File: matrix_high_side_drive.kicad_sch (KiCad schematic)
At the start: 28 parts

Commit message: [#72133] Unify sheet size
Signed-off-by: Dawid Lentka <dlentka@antmicro.com>
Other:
- title: (none) -> LED Panel Board
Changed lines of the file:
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@@
 	(generator_version "8.0")
 	(paper "A4")
+	(title_block
+		(title "LED Panel Board")
+		(date "28.01.2025")
+		(rev "1.0.0")
+	)
 	(junction
 		(at 58.42 41.91)

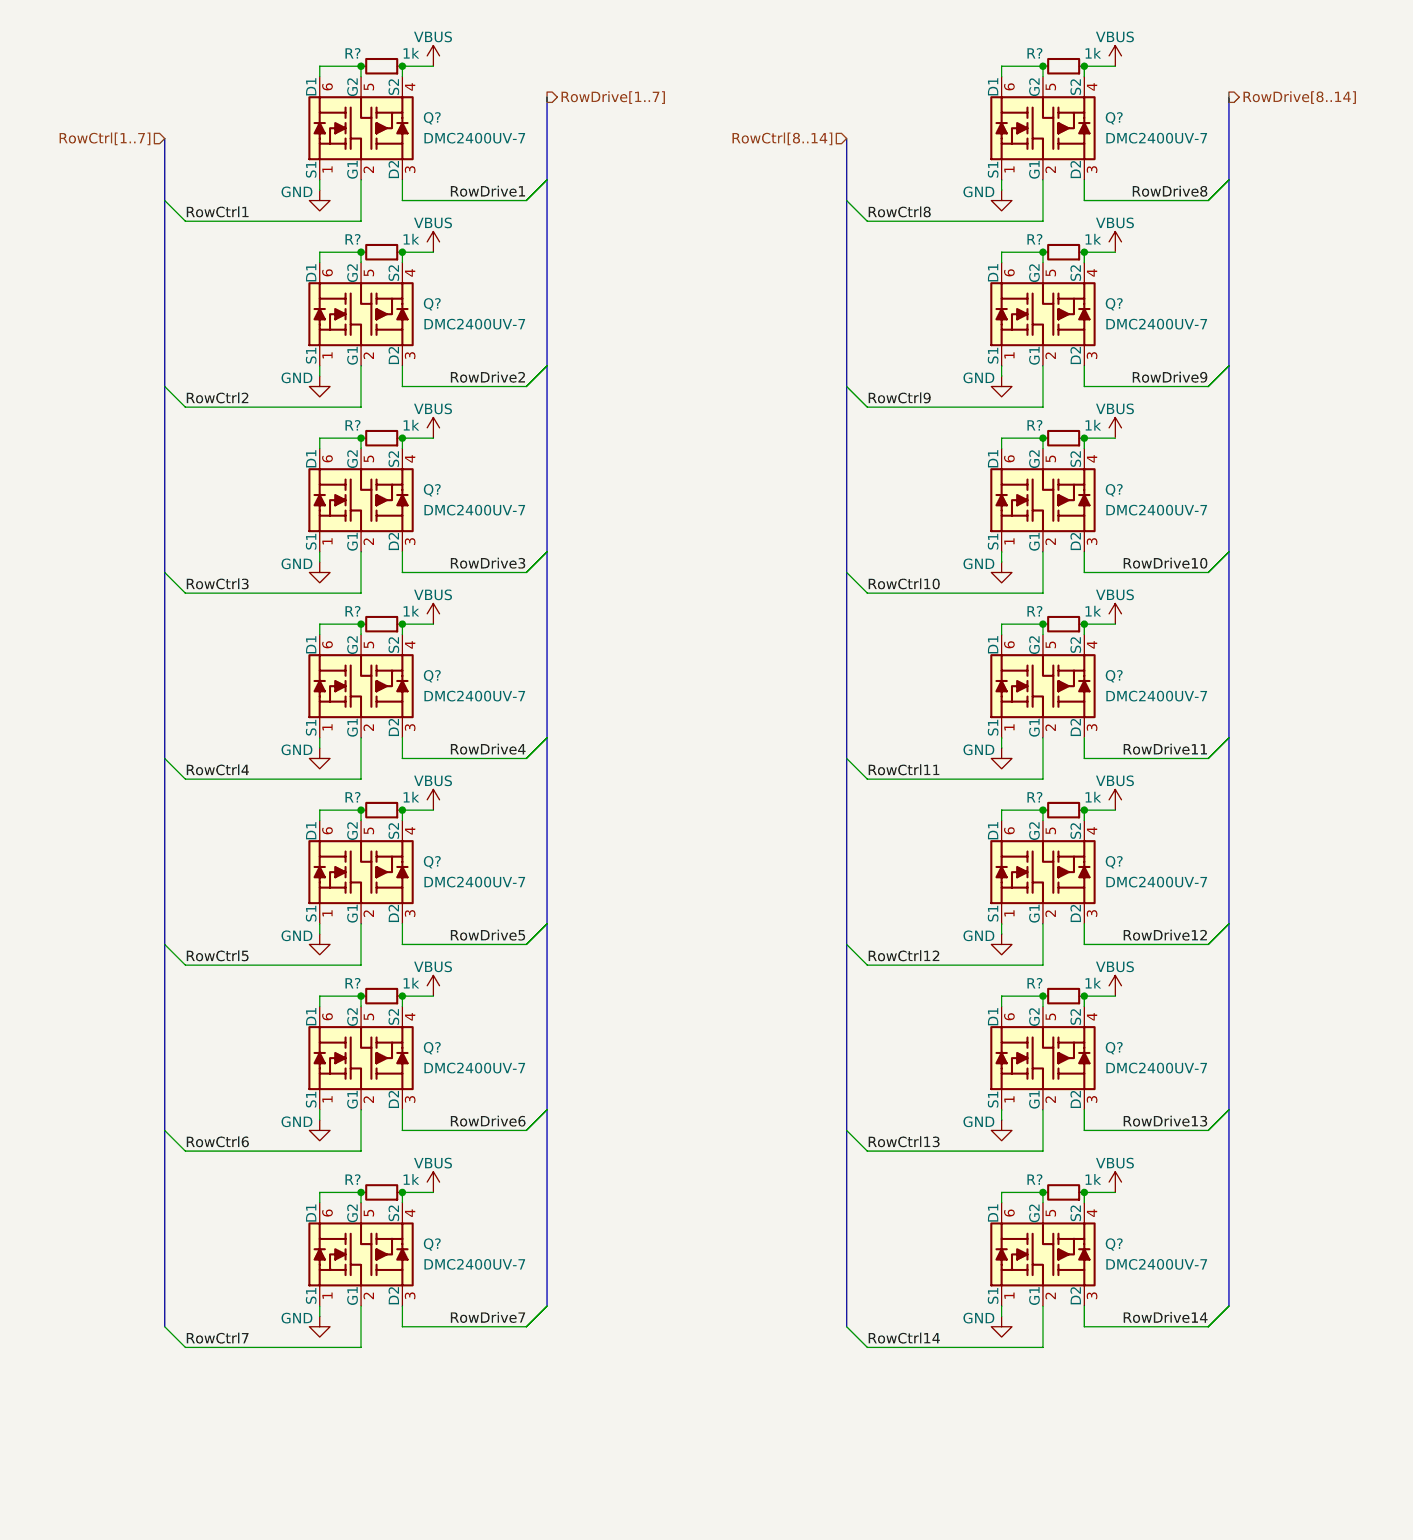
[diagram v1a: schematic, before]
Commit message: [#72133] Add capacitors on high side drive
Signed-off-by: Dawid Lentka <dlentka@antmicro.com>
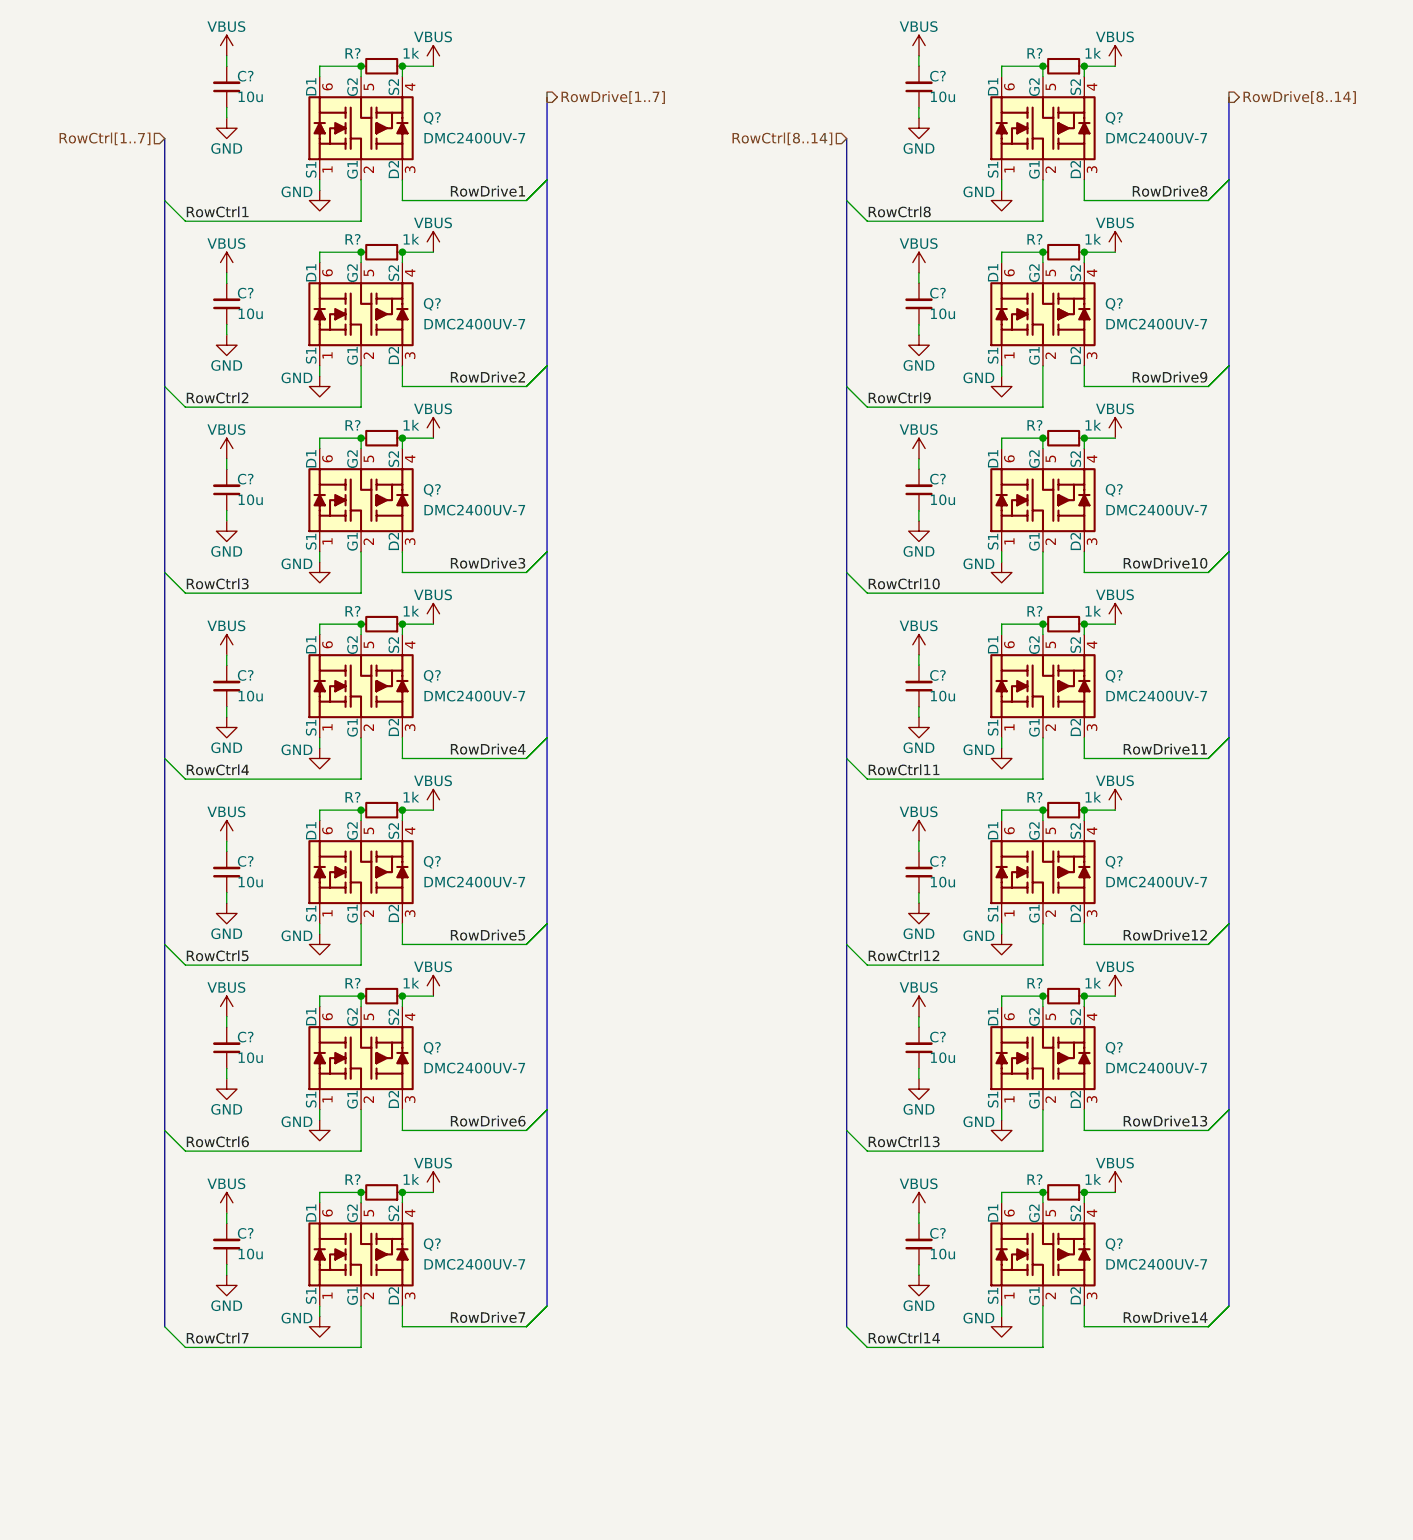
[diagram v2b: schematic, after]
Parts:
- added C? (x14): C_10u_10V_0402, antmicro-footprints:C_0402_1005Metric, symbol antmicroCapacitors0402:C_10u_10V_0402
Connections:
- net GND: now also C?.1, C?.1, C?.1, C?.1, C?.1, C?.1, C?.1, C?.1, C?.1, C?.1, C?.1, C?.1, C?.1, C?.1
- net VBUS: now also C?.2, C?.2, C?.2, C?.2, C?.2, C?.2, C?.2, C?.2, C?.2, C?.2, C?.2, C?.2, C?.2, C?.2

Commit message: [#72133] Add indicator LEDs & testpoints
Signed-off-by: Dawid Lentka <dlentka@antmicro.com>
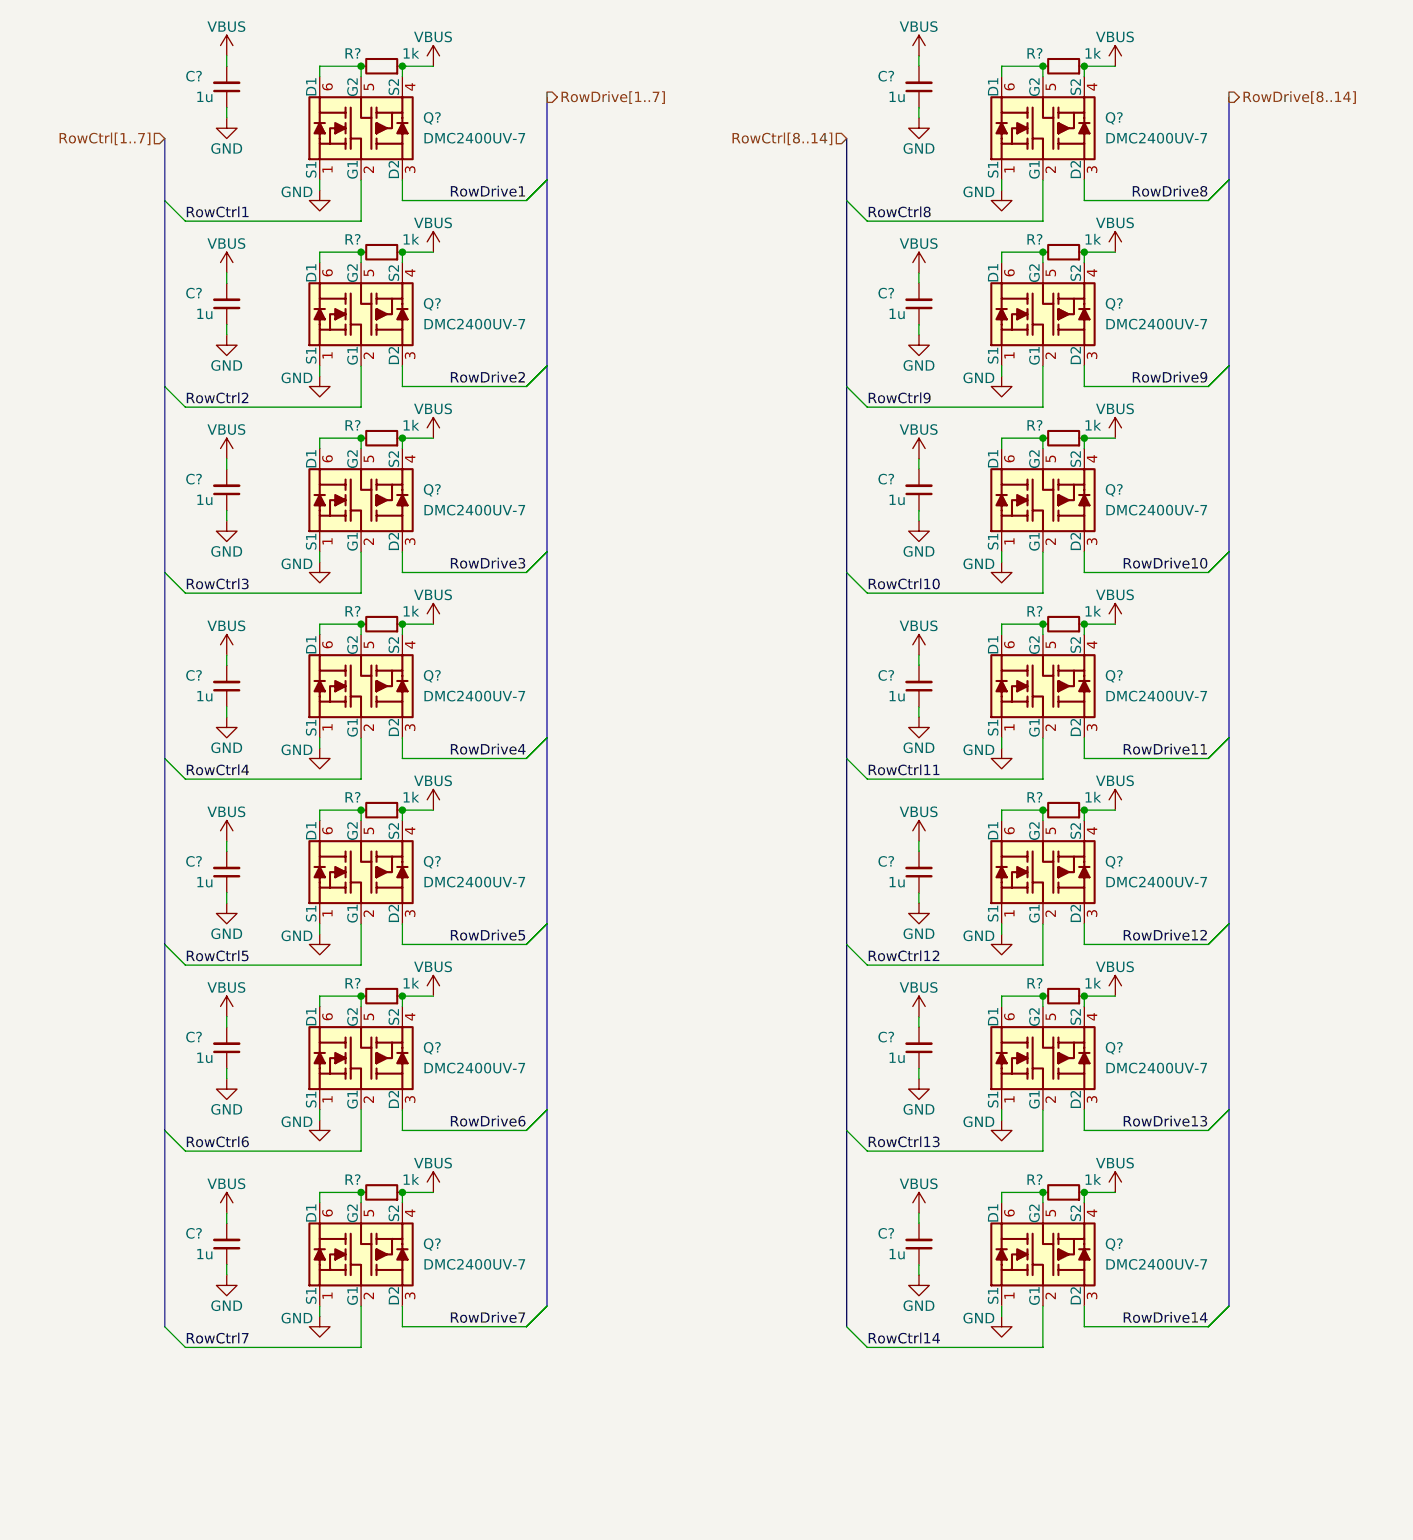
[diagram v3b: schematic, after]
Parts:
- removed C? (x14): C_10u_10V_0402, antmicro-footprints:C_0402_1005Metric, symbol antmicroCapacitors0402:C_10u_10V_0402
- added C? (x14): C_1u_16V_0402, antmicro-footprints:C_0402_1005Metric, symbol antmicroCapacitors0402:C_1u_16V_0402
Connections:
- net GND: now also C?.1, C?.1, C?.1, C?.1, C?.1, C?.1, C?.1, C?.1, C?.1, C?.1, C?.1, C?.1, C?.1, C?.1
- net VBUS: now also C?.2, C?.2, C?.2, C?.2, C?.2, C?.2, C?.2, C?.2, C?.2, C?.2, C?.2, C?.2, C?.2, C?.2

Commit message: [#72133] Annotate schematics
Signed-off-by: Dawid Lentka <dlentka@antmicro.com>
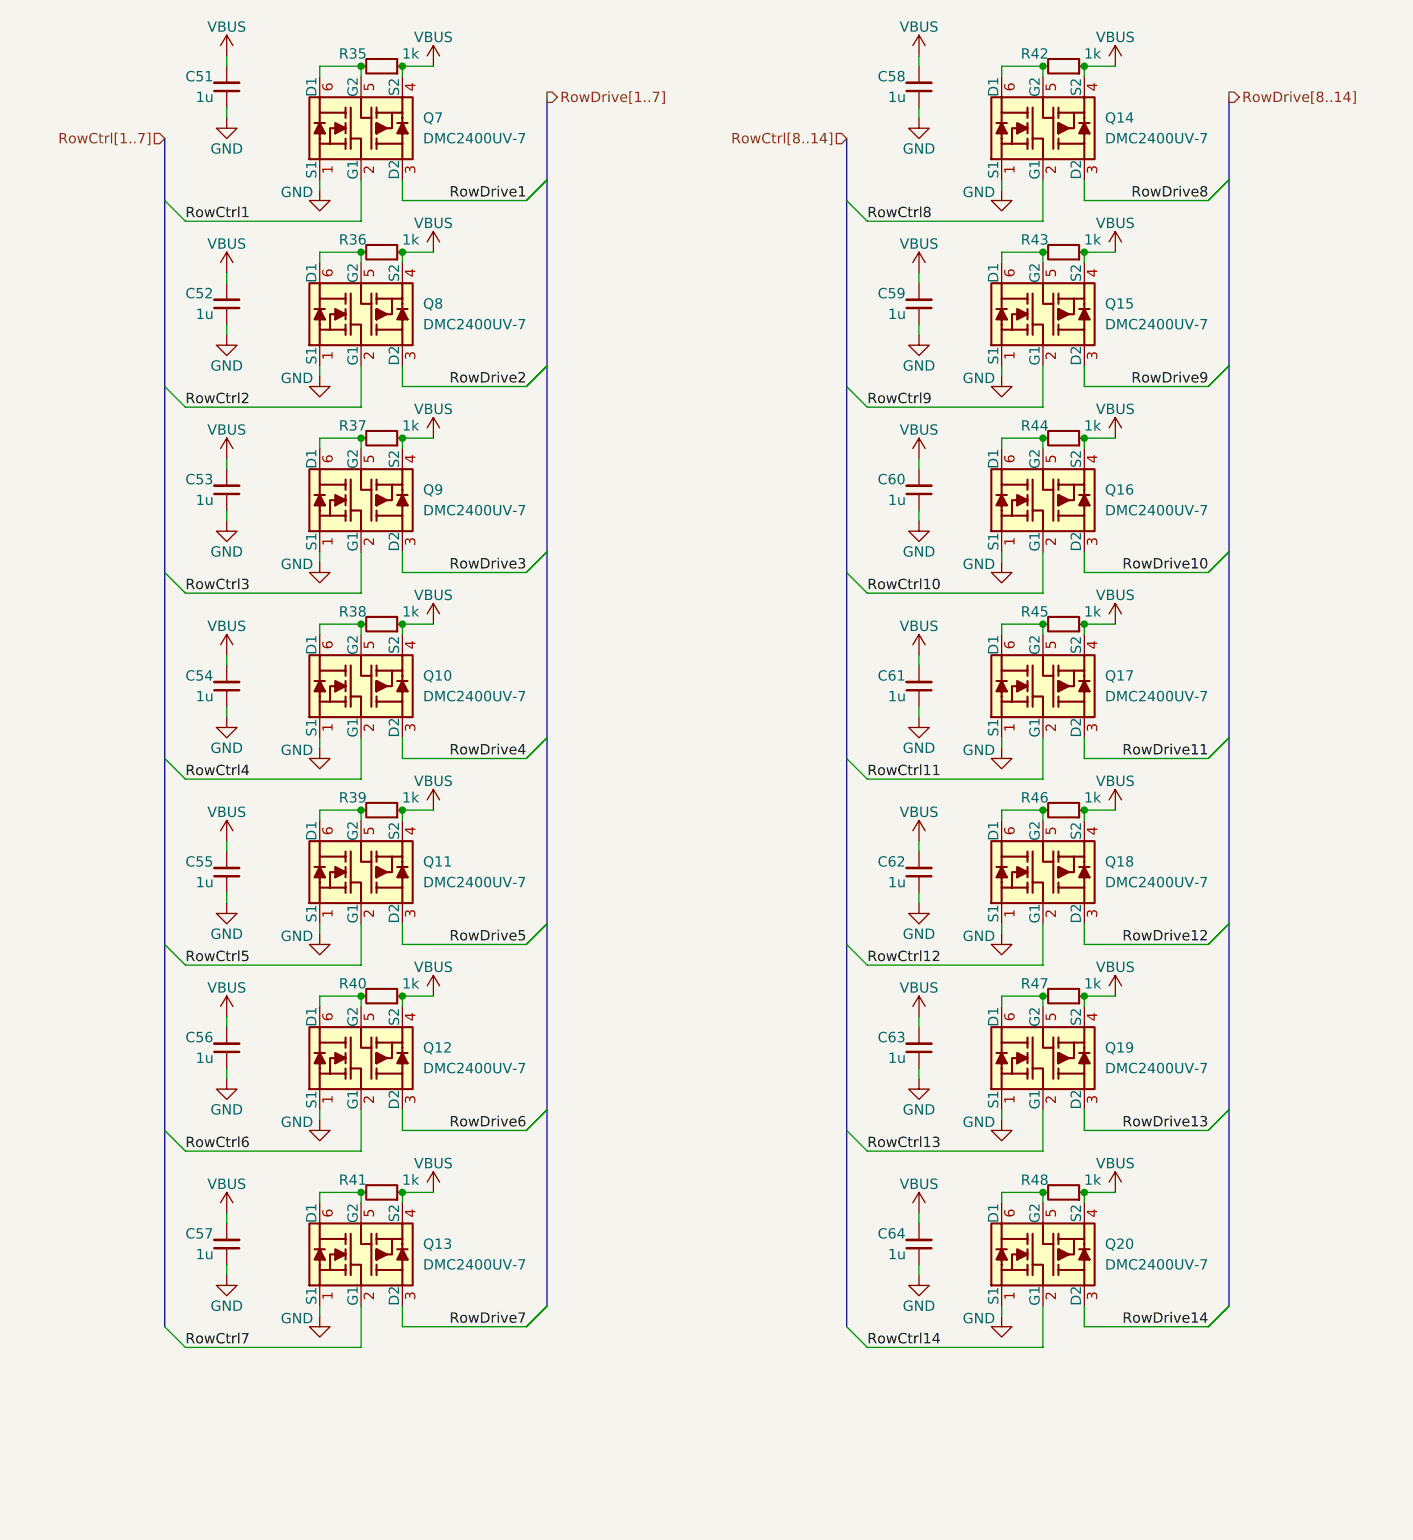
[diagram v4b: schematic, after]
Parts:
- gave numbers to parts that had none: 42

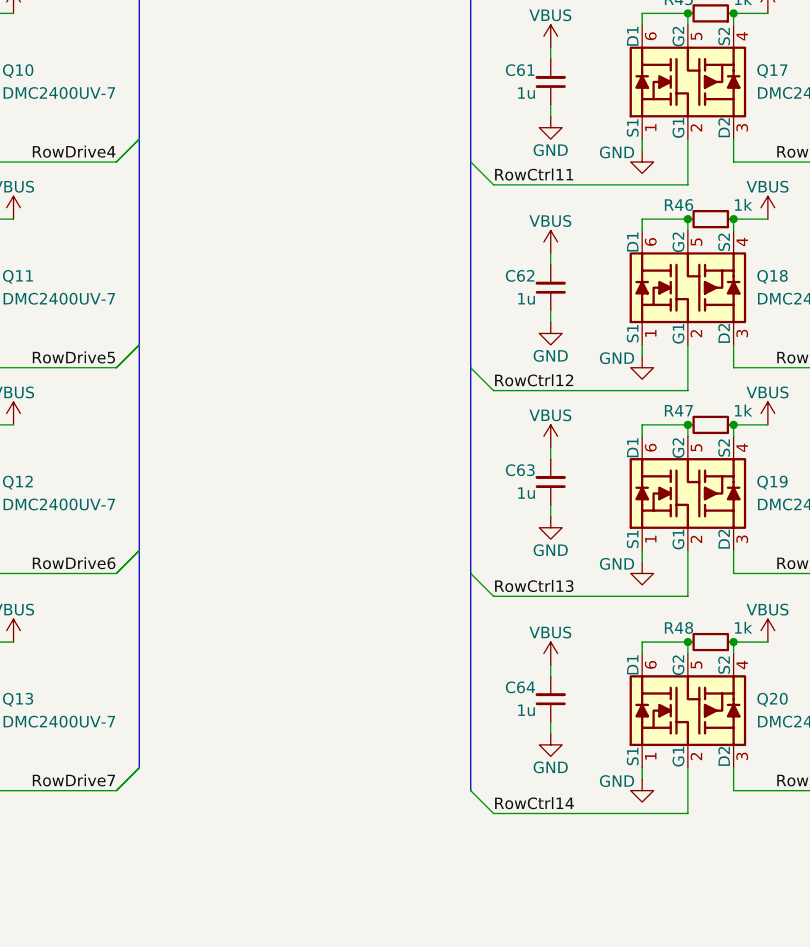
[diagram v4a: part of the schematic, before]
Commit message: [#72133] Sch: Update control hierarchy
Signed-off-by: Dawid Lentka <dlentka@antmicro.com>
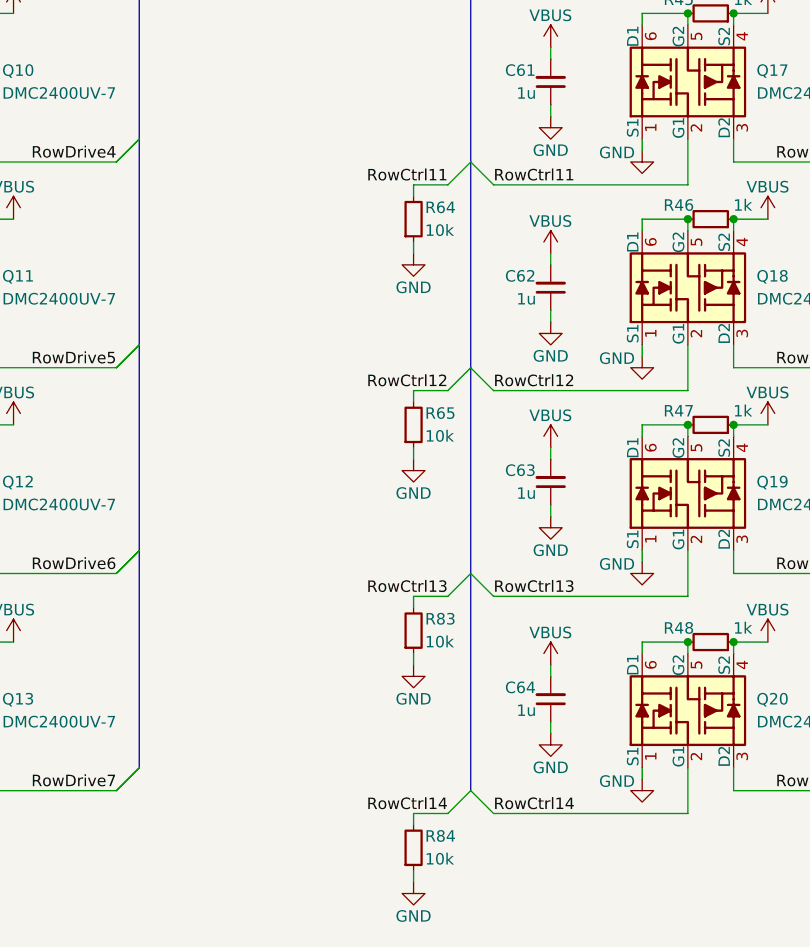
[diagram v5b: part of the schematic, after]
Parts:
- added R64, R65, R83, R84: R_10k_0402, antmicro-footprints:R_0402_1005Metric, symbol antmicroResistors0402:R_10k_0402
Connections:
- net GND: now also R64.1, R65.1, R83.1, R84.1
- net RowCtrl11: now also R64.2
- net RowCtrl12: now also R65.2
- net RowCtrl13: now also R83.2
- net RowCtrl14: now also R84.2
